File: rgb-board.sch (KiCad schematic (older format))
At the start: 91 parts, among them J1 Conn_02x25_Odd_Even, J10 RCJ-2223, J3 TEST_1P, J4 TEST_1P, J5 73415-3980, J6 73415-3980, J7 73415-3980, J8 73415-3980, J9 73415-3980, Q101 BC850C, Q105 BC850C, Q109 BC850C, Q113 BC850C, Q114 BC850C, Q201 BC850C, SW101 JS202011SCQN, SW105 JS202011SCQN, SW129 JS202011SCQN, SW143 JS202011SCQN, SW152 JS202011SCQN, U1 NCP1117-12_SOT223

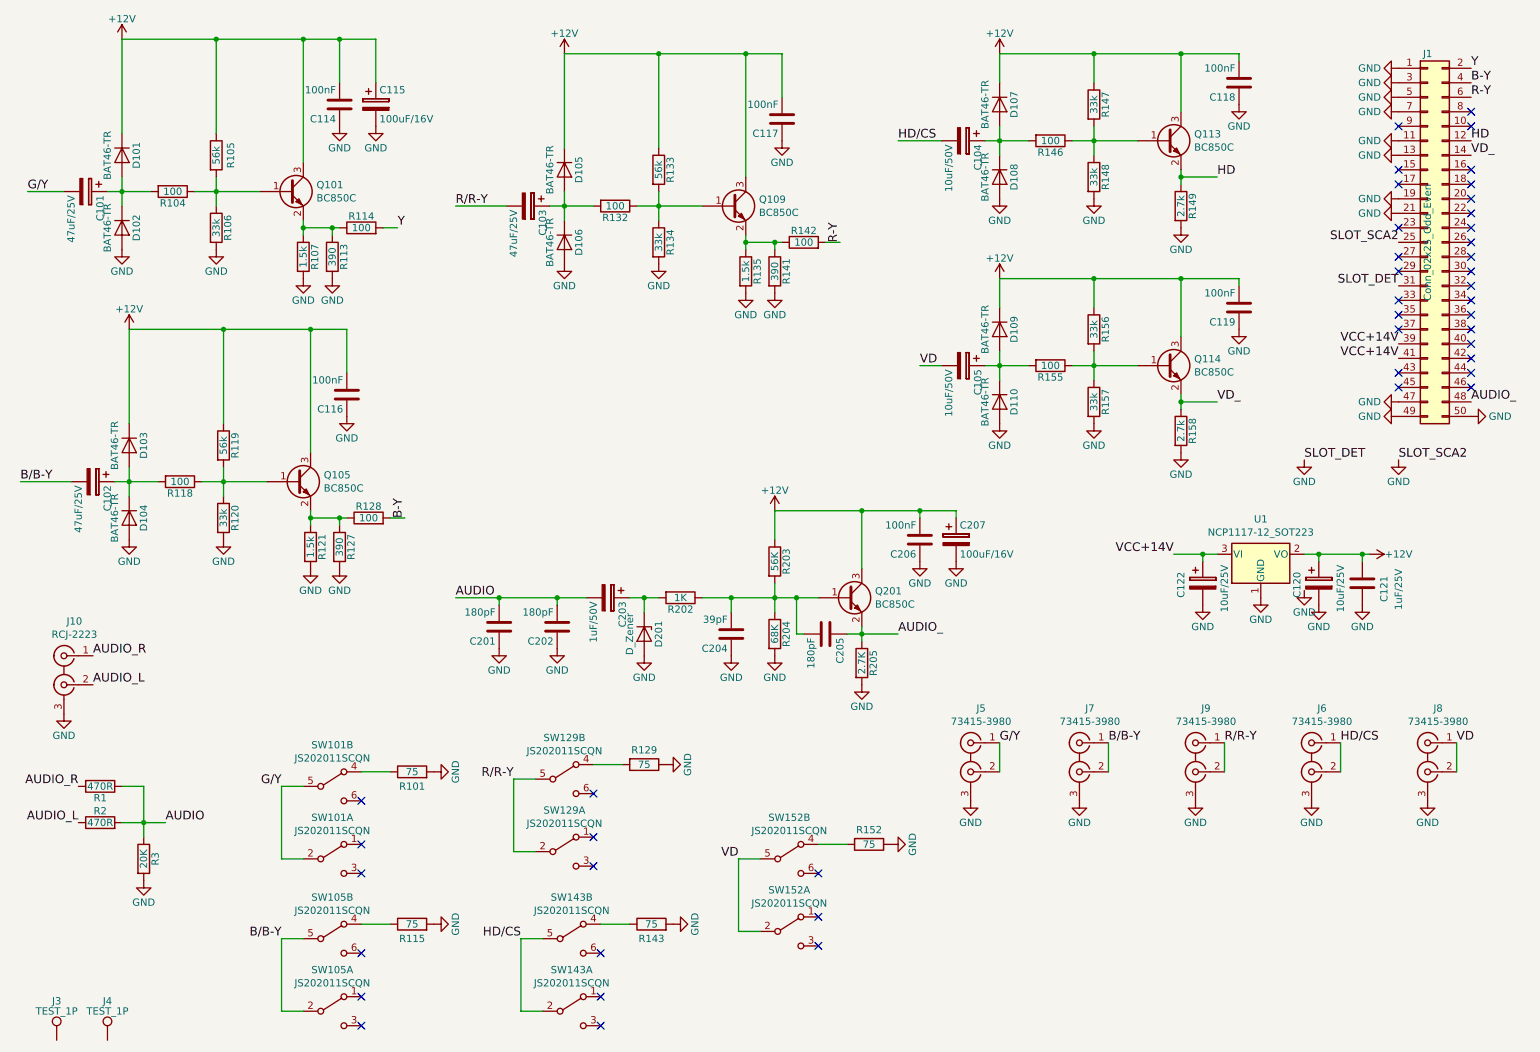
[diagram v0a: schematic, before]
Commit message: Add optional segments, update to Kicad 6
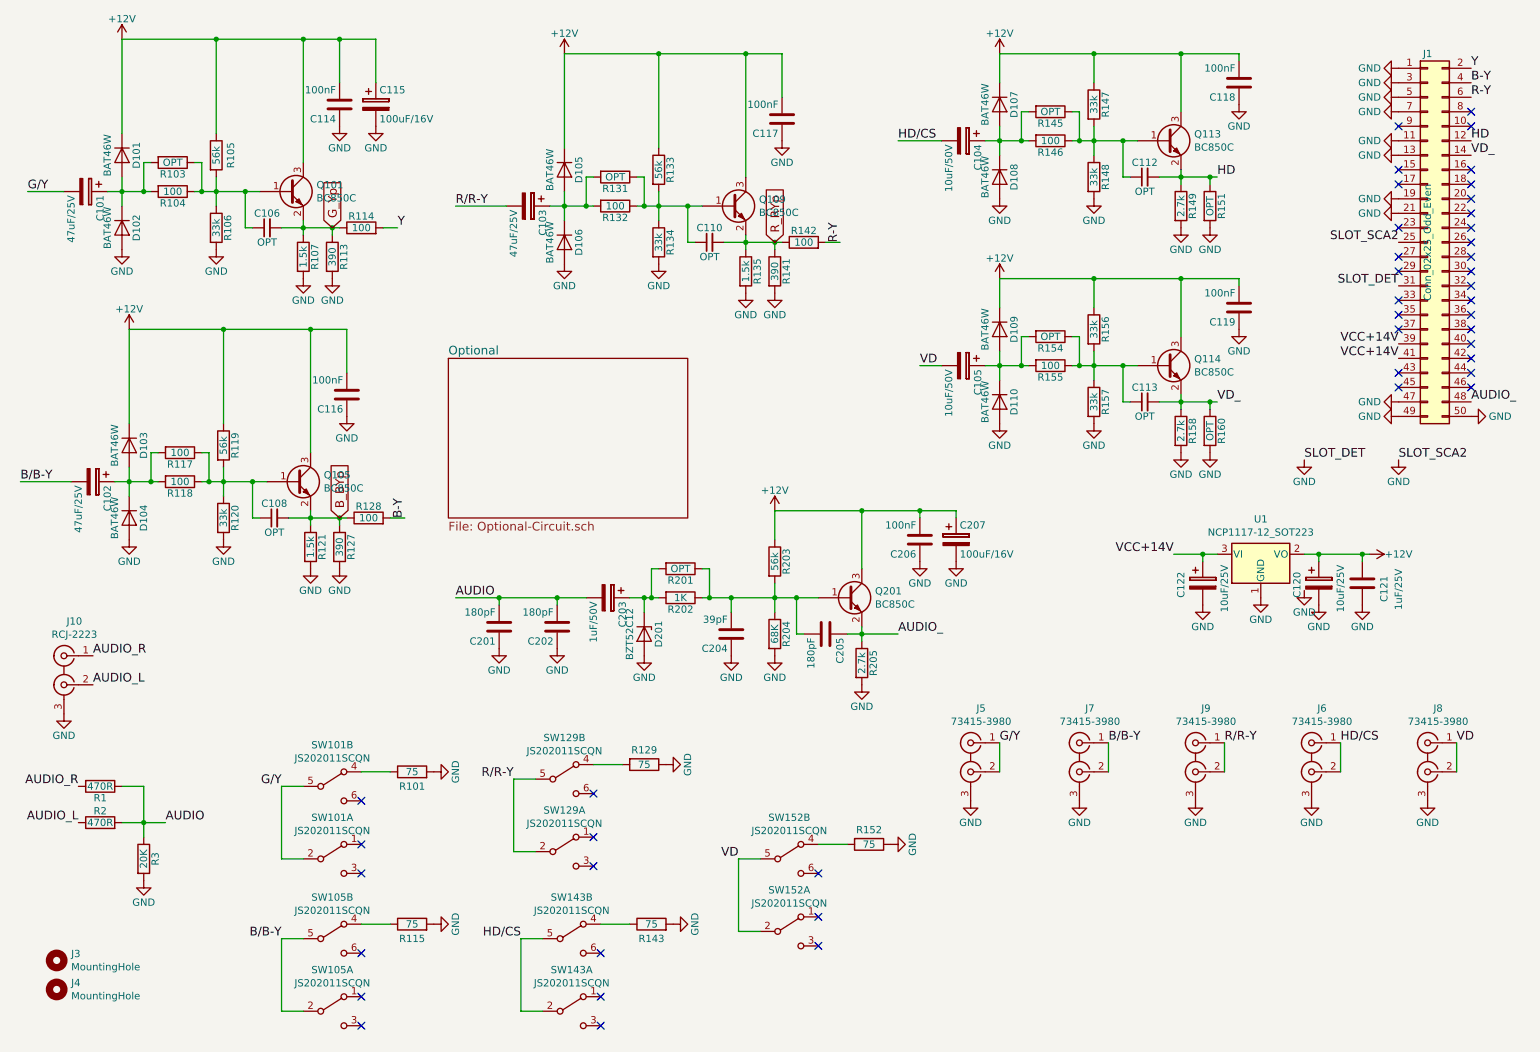
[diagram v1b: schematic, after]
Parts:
- removed J3, J4: TEST_1P, Mounting_Holes:MountingHole_3.2mm_M3, symbol rgb-board-rescue:TEST_1P
- added C106, C108, C110, C112, C113: OPT, Capacitor_SMD:C_0805_2012Metric_Pad1.18x1.45mm_HandSolder, symbol Device:C_Small
- added J3, J4: MountingHole, MountingHole:MountingHole_3.2mm_M3, symbol Mechanical:MountingHole
- added R103, R131, R145, R151, R154, R160, R201: OPT, Resistor_SMD:R_0805_2012Metric_Pad1.20x1.40mm_HandSolder, symbol rgb-board-rescue:R
- added R117: 100, Resistor_SMD:R_0805_2012Metric_Pad1.20x1.40mm_HandSolder, symbol rgb-board-rescue:R
- C101, C102, C103: JLC (none) -> SMD,6.3x6.1mm; LCSC (none) -> C88810
- C104, C105, C120, C122: JLC (none) -> SMD,5x5.4mm; LCSC (none) -> C445070
- C114, C116, C117, C118, C119, C206: JLC (none) -> 0805; LCSC (none) -> C1711
- C115, C207: JLC (none) -> SMD,6.3x7.7mm; LCSC (none) -> C125975
- C121: JLC (none) -> 0805; LCSC (none) -> C28323
- C201, C202, C205: JLC (none) -> 0805; LCSC (none) -> C113826
- C203: JLC (none) -> SMD,4x5.8mm; LCSC (none) -> C2163317
- C204: JLC (none) -> 0805; LCSC (none) -> C527185
- D101, D102, D103, D104, D105, D106, D107, D108, D109, D110: value BAT46-TR -> BAT46W; JLC (none) -> SOD-123; LCSC (none) -> C83152
- D201: value D_Zener -> BZT52C12; JLC (none) -> SOD-123; LCSC (none) -> C177013
- Q101, Q105, Q109, Q113, Q114, Q201: JLC (none) -> SOT-23(SOT-23-3); LCSC (none) -> C78484
- R1, R2: JLC (none) -> 0805; LCSC (none) -> C114564
- R101, R115, R129, R143, R152: JLC (none) -> 0805; LCSC (none) -> C141697
- R104, R114, R118, R128, R132, R142, R146, R155: JLC (none) -> 0805; LCSC (none) -> C105577
- R105, R119, R133: JLC (none) -> 0805; LCSC (none) -> C137509
- R106, R120, R134, R147, R148, R156, R157: JLC (none) -> 0805; LCSC (none) -> C141696
- R107, R121, R135: JLC (none) -> 0805; LCSC (none) -> C114555
- R113, R127, R141: JLC (none) -> 0805; LCSC (none) -> C114543
- R149, R158: JLC (none) -> 0805; LCSC (none) -> C144567
- R202: JLC (none) -> 0805; LCSC (none) -> C95781
- R203: value 56K -> 56k; JLC (none) -> 0805; LCSC (none) -> C137509
- R204: JLC (none) -> 0805; LCSC (none) -> C228958
- R205: value 2.7K -> 2.7k; JLC (none) -> 0805; LCSC (none) -> C144567
- R3: JLC (none) -> 0805; LCSC (none) -> C114566
- SW101, SW105, SW129, SW143, SW152: JLC (none) -> SMD; LCSC (none) -> C221666
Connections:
- net GND: now also R151.2, R160.2
- net HD: now also C112.2, R151.1
- net VD_: now also C113.2, R160.1
- net at C101.1, D101.2 (A), D102.1 (K)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: now also R103.2
- net at Q101.1 (B), R104.1, R105.2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: now also C106.1, R103.1
- net G_Yp: now reaches Q101.2 (E), R107.1, R113.1, R114.1
- net G_Yp: now also C106.2
- net at C102.1, D103.2 (A), D104.1 (K)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: now also R117.2
- net at Q105.1 (B), R118.1, R119.2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: now also C108.1, R117.1
- net B_BYp: now reaches Q105.2 (E), R121.1, R127.1, R128.1
- net B_BYp: now also C108.2
- net at C103.1, D105.2 (A), D106.1 (K)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: now also R131.2
- net at Q109.1 (B), R132.1, R133.2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: now also C110.1, R131.1
- net R_RYp: now reaches Q109.2 (E), R135.1, R141.1, R142.1
- net R_RYp: now also C110.2
- net at C104.1, D107.2 (A), D108.1 (K)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: now also R145.2
- net at Q113.1 (B), R146.1, R147.2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: now also C112.1, R145.1
- net at C105.1, D109.2 (A), D110.1 (K)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: now also R154.2
- net at Q114.1 (B), R155.1, R156.2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: now also C113.1, R154.1
- net at C203.1, D201.1 (K), R202.2: now also R201.2
- net at C204.2, C205.2, Q201.1 (B)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: now also R201.1
